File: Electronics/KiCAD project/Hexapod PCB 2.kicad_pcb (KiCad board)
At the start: 4 copper layers, 53 x 85 mm, 79 parts, among them J1 XT60, J2 leg1, J3 leg2, J4 leg3, J5 leg4, J6 leg5, J7 leg6, J8 USB_C_Receptacle_USB2.0_16P, Q1 IRF4905, Q2 Q_NPN_BCE, Q3 Q_NPN_BCE, SW2 SW_SPST, SW3 SW_SPST, U1 TPS563201, U2 TPS563201, U3 ESP32-S3-WROOM-1, U4 USBLC6-2P6, U5 BNO055, U6 INA226

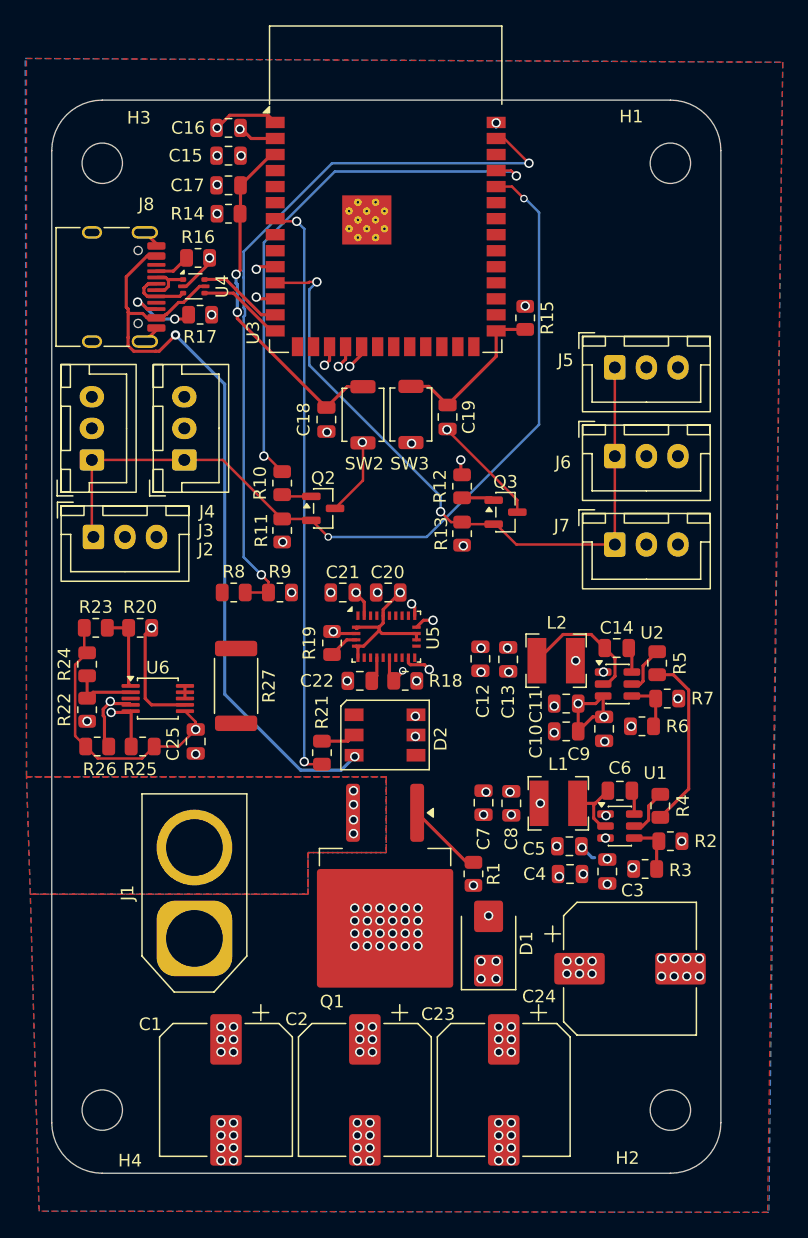
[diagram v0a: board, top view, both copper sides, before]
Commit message: update PCB, BOM, README, add firmware
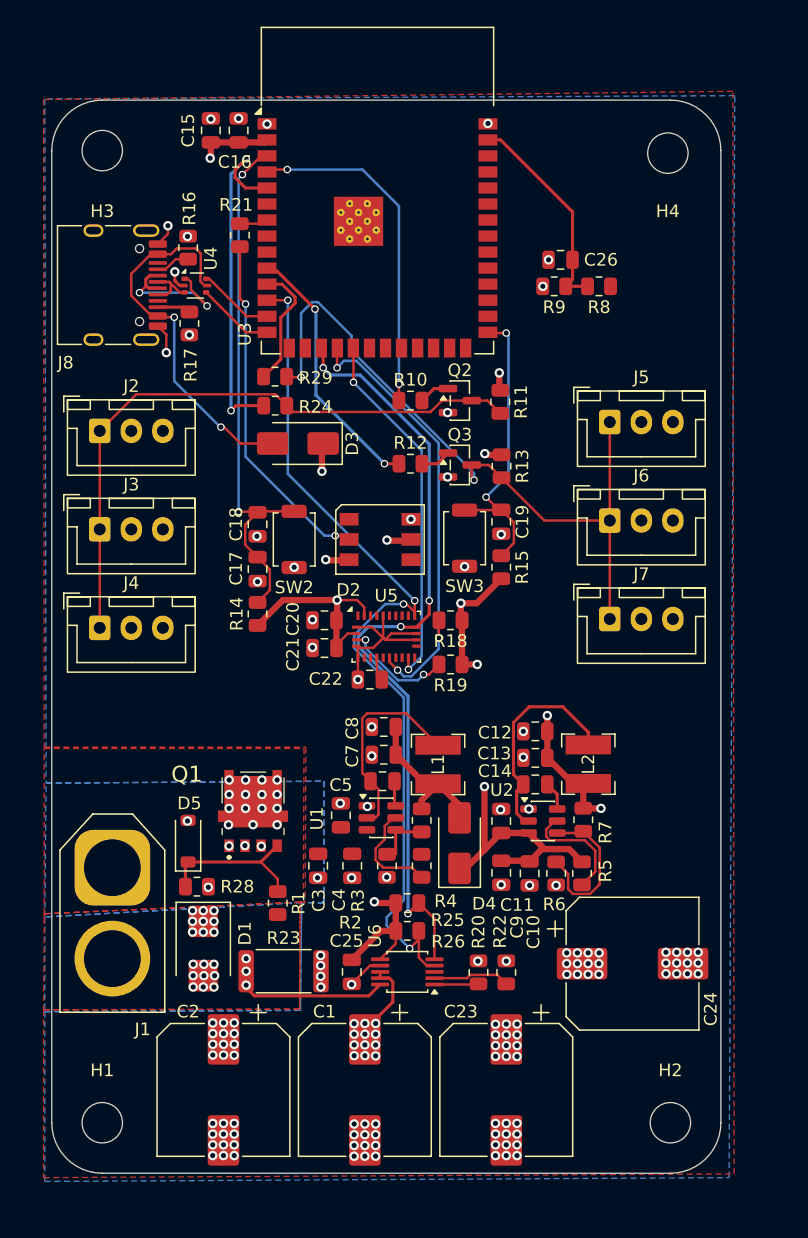
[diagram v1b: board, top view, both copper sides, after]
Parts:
- removed R27: RS, Resistor_SMD:R_2512_6332Metric
- added C26: 0.1uF, Capacitor_SMD:C_0805_2012Metric, F.Cu at (169.7, 75.5)
- added D3: SS34, Diode_SMD:D_SMA, F.Cu at (148.9, 90.0)
- added D4: SS34, Diode_SMD:D_SMA, F.Cu at (161.7, 121.7)
- added D5: BZT52C12, Diode_SMD:D_SOD-123, F.Cu at (140.2, 121.5)
- added R28: 100k, Resistor_SMD:R_0805_2012Metric, F.Cu at (140.9, 125.1)
- added R29: 1k, Resistor_SMD:R_0805_2012Metric, F.Cu at (147.1, 84.7)
- D1: value D_TVS -> SMBJ10CA
- Q1: value IRF4905 -> NTMFS5C404NLT1G; footprint Package_TO_SOT_SMD:TO-263-2 -> n-mosfet:NTMFS4C022N
- Q2, Q3: value Q_NPN_BCE -> MMBT3904
- R1: value 100k -> 10k
- R2: value 54.9k -> 59k
- R23: value 10k -> 2m; footprint Resistor_SMD:R_0805_2012Metric -> Resistor_SMD:R_2512_6332Metric
- R24: value 10k -> 1k
- R8: value 51k -> 100k
- moved H1 88.3 mm to (133.4, 143.8)
- moved H4 88.0 mm to (178.2, 67.0)
- moved R21 41.5 mm to (144.3, 73.5), turned to 90 degrees
- moved R22 39.2 mm to (165.4, 131.9), turned to 90 degrees
- moved R20 38.2 mm to (163.2, 131.9), turned to 90 degrees
- moved R8 37.8 mm to (172.8, 77.5), turned to 180 degrees
- moved R9 32.6 mm to (169.2, 77.5), turned to 180 degrees
- moved R14 31.8 mm to (145.7, 103.5), turned to 90 degrees
- moved R23 31.0 mm to (147.8, 131.8)
- moved C17 30.5 mm to (145.7, 100.0), turned to -90 degrees
- moved U6 29.3 mm to (157.6, 131.8), turned to 180 degrees
- moved R26 28.6 mm to (157.6, 128.6)
- moved R24 25.3 mm to (147.1, 87.0), turned to 0 degrees
- moved R25 24.4 mm to (157.6, 126.4), turned to 180 degrees
- moved C3 22.9 mm to (150.5, 123.5)
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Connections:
- C7 pad 2: +5V -> 5v_buck
- C8 pad 2: +5V -> 5v_buck
- D1 pad 1: GND -> +BATT
- D1 pad 2: SERVO-POWER -> GND
- J1 pad 1: GND -> -BATT
- J8 pad A4: +5V -> Net-(D3-A)
- J8 pad A9: +5V -> Net-(D3-A)
- J8 pad B4: +5V -> Net-(D3-A)
- J8 pad B9: +5V -> Net-(D3-A)
- L1 pad 2: +5V -> 5v_buck
- Q1 pad 1: Net-(Q1-G) -> GND
- Q1 pad 2: SERVO-POWER -> GND
- Q1 pad 3: +BATT -> GND
- Q2 pad 2: BUS1 -> GND
- Q2 pad 3: GND -> BUS1
- Q3 pad 2: BUS2 -> GND
- Q3 pad 3: GND -> BUS2
- R1 pad 1: GND -> Net-(D5-K)
- R1 pad 2: Net-(Q1-G) -> +BATT
- R2 pad 2: +5V -> 5v_buck
- R23 pad 1: +3.3V -> +BATT
- R23 pad 2: Net-(U6-A1) -> SERVO-POWER
- R24 pad 1: +3.3V -> Net-(U3-IO5)
- R24 pad 2: Net-(U6-A0) -> BUS1
- R4 pad 1: EN -> SERVO-POWER
- R5 pad 1: EN -> +5V
- U3 pad 11: BUS2 -> Net-(U3-IO18)
- U3 pad 36: BUS1 -> unconnected-(U3-RXD0-Pad36)
- U3 pad 37: TX1 -> unconnected-(U3-TXD0-Pad37)
- U3 pad 4: unconnected-(U3-IO4-Pad4) -> TX1
- U3 pad 5: unconnected-(U3-IO5-Pad5) -> Net-(U3-IO5)
- U4 pad 5: +5V -> Net-(D3-A)
- U6 pad 10: SERVO-POWER -> +BATT
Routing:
- net +3.3V: track 30.2 -> 148.7 mm, vias 15 -> 9
- net STAT_LED: track 46.3 -> 2.27 mm, vias 2 -> 0
- net VBATT-SENSE: track 58.6 -> 16.9 mm, vias 2 -> 0
- net Net-(D3-A): track 0.00 -> 30.1 mm, vias 0 -> 2
- net Net-(U3-IO5): track 0.00 -> 27.9 mm, vias 0 -> 2
- net GND: track 51.1 -> 23.6 mm, vias 69 -> 101
- net Net-(D2-DIN): track 2.75 -> 27.7 mm, vias 0 -> 2
- net BUS1: track 68.8 -> 49.9 mm, vias 2 -> 0
- net TX1: track 43.1 -> 27.1 mm
- net Net-(SW2-A): track 28.1 -> 42.6 mm
- net EN: track 14.0 -> 0.00 mm
- net Net-(D5-K): track 0.00 -> 12.5 mm
- net 5v_buck: track 0.00 -> 12.4 mm
- net +BATT: track 0.07 -> 11.3 mm, vias 4 -> 12
- net Net-(U1-SW): track 5.24 -> 16.4 mm
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- added copper zone on B.Cu, net -BATT
- added copper zone on F.Cu, net -BATT
- added copper zone on In2.Cu, net GND
- removed copper zone on In2.Cu, net +3.3V
- removed copper zone on In2.Cu, net +5V
